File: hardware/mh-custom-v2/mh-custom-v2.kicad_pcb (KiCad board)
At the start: 2 copper layers, 95.7 x 99.3 mm, 113 parts, among them J1 Conn_01x03_Male, J10 Screw_Terminal_01x02, J11 Screw_Terminal_01x02, J12 Screw_Terminal_01x02, J3 Conn_02x19_Top_Bottom, J4 Conn_02x19_Top_Bottom, J5 Screw_Terminal_01x02, J6 Screw_Terminal_01x02, J7 Screw_Terminal_01x02, J8 Screw_Terminal_01x02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

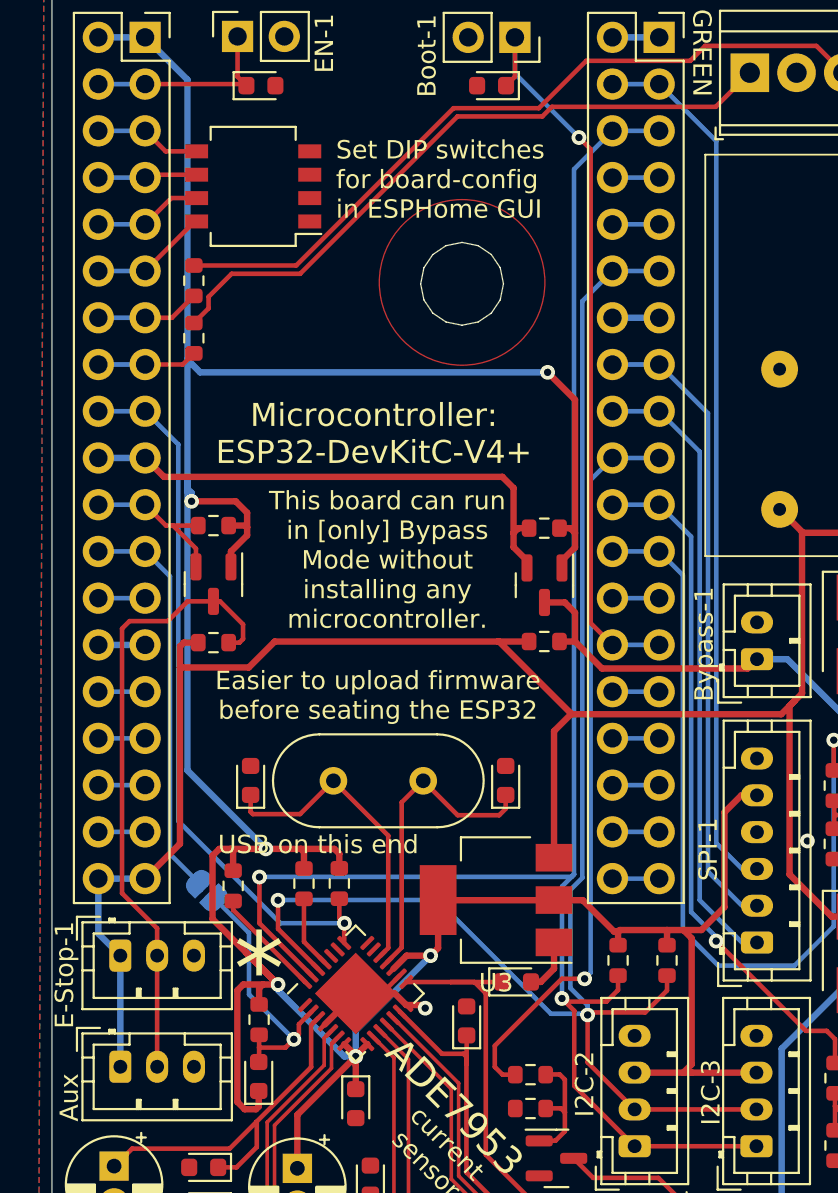
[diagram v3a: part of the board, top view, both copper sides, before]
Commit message: added jumpers that allow for two seperate E-Stop readings
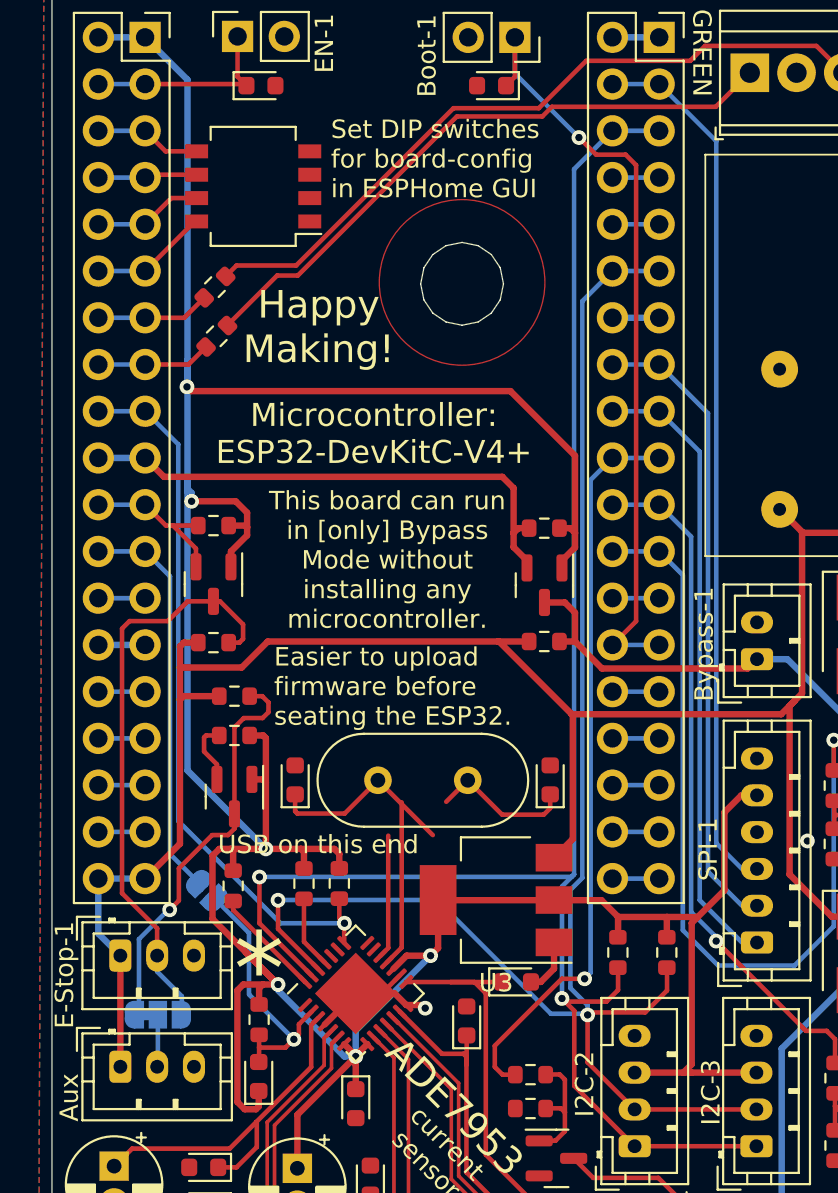
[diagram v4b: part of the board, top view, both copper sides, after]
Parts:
- added JP14: SolderJumper_3_Bridged12, Jumper:SolderJumper-3_P1.3mm_Bridged12_RoundedPad1.0x1.5mm, B.Cu at (38.7, 78.2)
- added R34: 10k, Resistor_SMD:R_0603_1608Metric, F.Cu at (42.9, 63.1)
- added R35: 10k, Resistor_SMD:R_0603_1608Metric, F.Cu at (42.9, 60.9)
- added T6: AO3400A, Package_TO_SOT_SMD:SOT-23, F.Cu at (42.9, 66.4)
- R7, R8: value 10kOhm -> 2.2k
- moved C20 2.42 mm to (46.2, 65.5)
- moved C21 2.42 mm to (60.0, 65.5)
- moved Y1 2.42 mm to (53.1, 65.5)
- moved R6 1.25 mm to (41.9, 41.4), turned to -135 degrees
- moved R5 1.20 mm to (41.8, 38.7), turned to 45 degrees
- moved R8 0.43 mm to (63.7, 74.9)
- moved R7 0.43 mm to (66.4, 74.9)
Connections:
- E-Stop-2 pad 2: Net-(E-Stop-1-Pad2) -> Net-(E-Stop-2-Pad2)
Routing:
- net Net-(JP14-Pad1): track 0.00 -> 22.3 mm, vias 0 -> 1
- net +3V3: track 194.4 -> 201.5 mm
- net read-aux-E-Stop: track 0.00 -> 3.44 mm
- net Net-(E-Stop-2-Pad2): track 0.00 -> 2.85 mm
- net +5V: track 162.2 -> 164.5 mm
- net Net-(E-Stop-1-Pad2): track 34.0 -> 31.7 mm
- net Net-(J1-Pad1): track 36.2 -> 34.1 mm
- net boot: track 40.6 -> 42.6 mm
- net Net-(J1-Pad3): track 40.9 -> 39.4 mm
- net led-grn: track 5.44 -> 6.58 mm
- net led-red: track 5.68 -> 6.20 mm
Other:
- board text added: "Easier to upload firmware before seating the ESP32."
- board text added: "Happy Making!"
- board text added: "also swap"
- board text removed: "Easier to upload firmware before seating the ESP32"

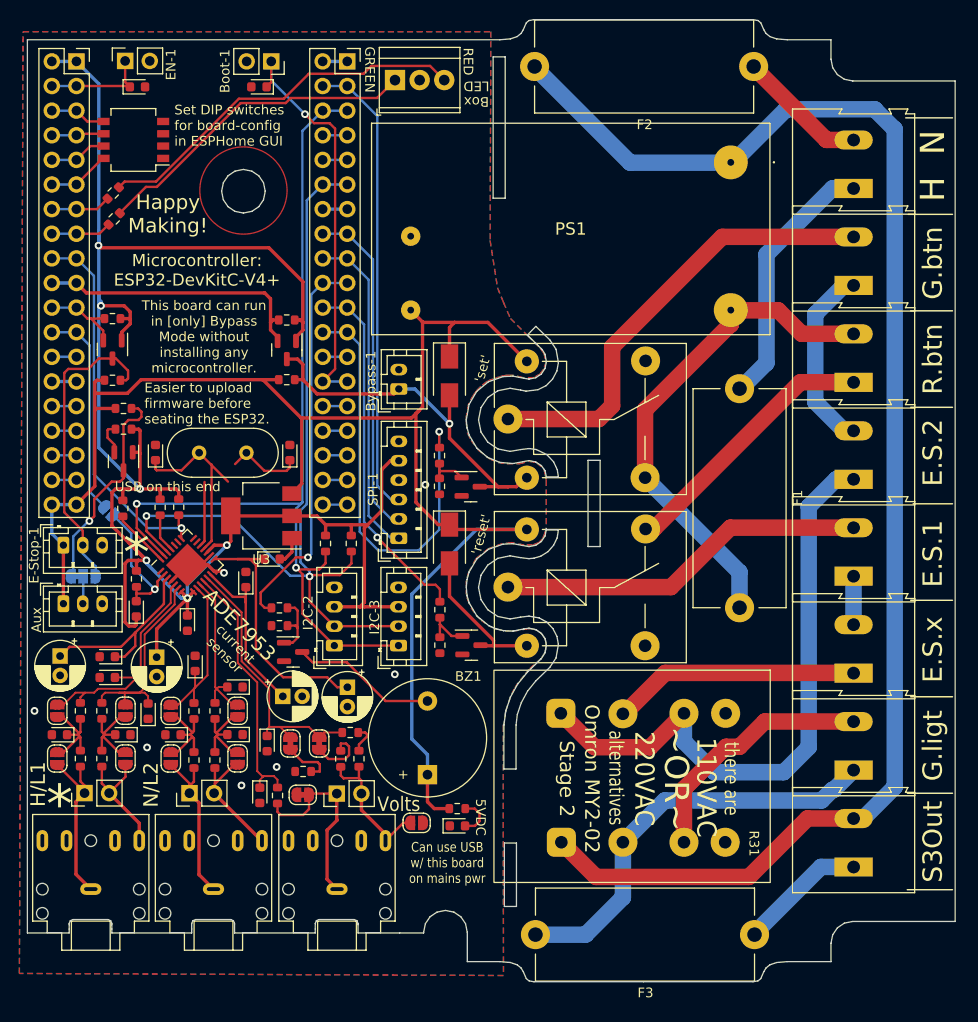
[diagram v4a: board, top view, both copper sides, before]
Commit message: b-silkscreen fixed
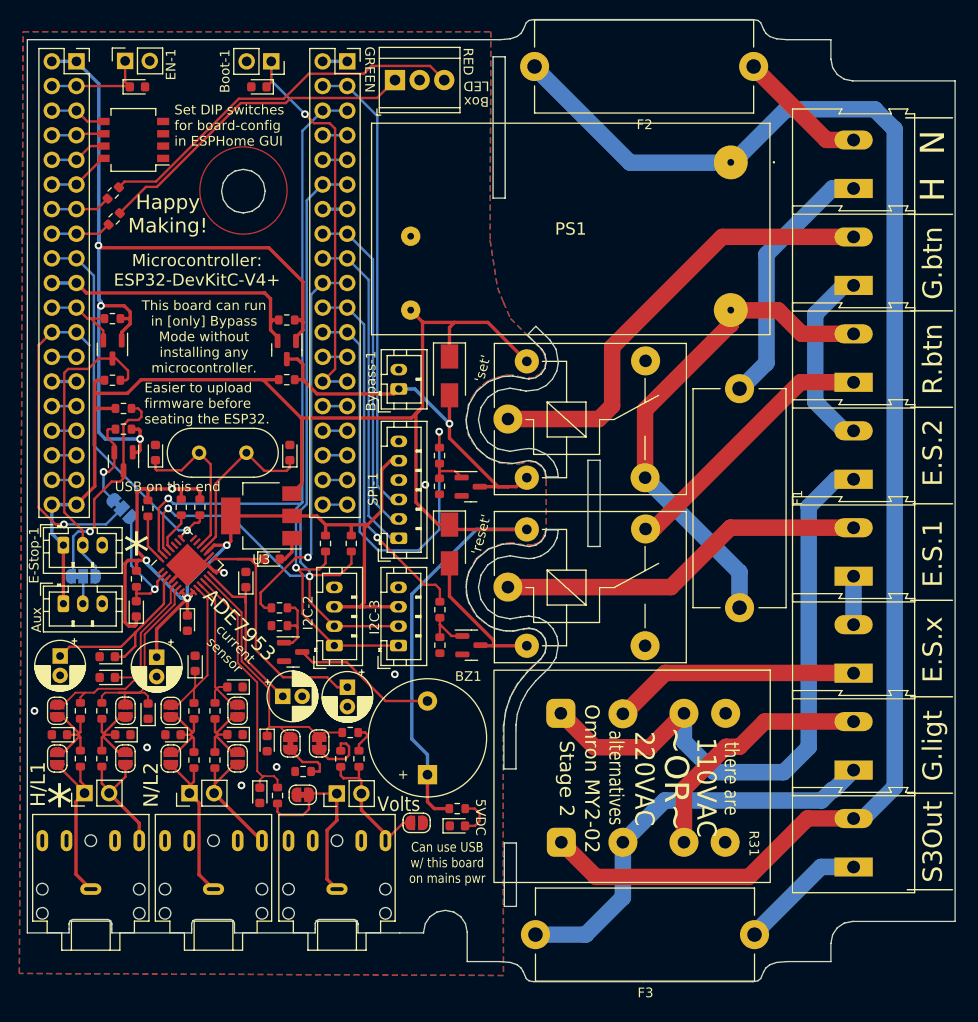
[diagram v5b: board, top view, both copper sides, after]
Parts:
- JP13: value software-reset -> SolderJumper_3_Bridged12; footprint Jumper:SolderJumper-2_P1.3mm_Open_RoundedPad1.0x1.5mm -> Jumper:SolderJumper-3_P1.3mm_Bridged12_RoundedPad1.0x1.5mm
- moved R24 2.59 mm to (45.4, 71.2)
- moved R23 2.18 mm to (50.7, 71.1)
- moved R25 2.18 mm to (48.8, 71.1)
- moved JP13 1.35 mm to (42.7, 71.2)
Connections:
- J3 pad 23: ade7953-reset -> two-options
- J3 pad 24: ade7953-reset -> two-options
- JP13 pad 1: ade7953-reset -> read-aux-E-Stop
- JP13 pad 2: Net-(C15-Pad2) -> two-options
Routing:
- net two-options: track 0.00 -> 33.1 mm, vias 0 -> 1
- net ade7953-reset: track 21.7 -> 0.00 mm
- net +3V3: track 201.5 -> 190.5 mm, vias 6 -> 7
- net read-aux-E-Stop: track 3.44 -> 9.50 mm, vias 0 -> 1
- net SCL: track 95.0 -> 92.0 mm
- net SDA: track 86.8 -> 85.2 mm
- net CS: track 6.02 -> 4.95 mm
- net Net-(C21-Pad1): track 16.8 -> 17.9 mm
- net Net-(C15-Pad2): track 14.8 -> 13.9 mm
- net Net-(JP14-Pad1): track 22.3 -> 23.0 mm
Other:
- board text added: "Read 2 EStops or ADE7953 reset"
- board text removed: "ADE7953 reset pin connect"

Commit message: applied workaround for 3.3v and 3v3 known bug: https://gitlab.com/kicad/libraries/kicad-symbols/-/issues/3153
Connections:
- C13 pad 1: +3V3 -> +3.3V
- C14 pad 1: +3V3 -> +3.3V
- C15 pad 1: +3V3 -> +3.3V
- I2C-2 pad 3: +3V3 -> +3.3V
- I2C-3 pad 3: +3V3 -> +3.3V
- J3 pad 1: +3V3 -> +3.3VA
- J3 pad 2: +3V3 -> +3.3VA
- R22 pad 2: +3V3 -> +3.3V
- R23 pad 2: +3V3 -> +3.3V
- R24 pad 2: +3V3 -> +3.3V
- R25 pad 2: +3V3 -> +3.3V
- R3 pad 2: +3V3 -> +3.3VA
- R32 pad 2: +3V3 -> +3.3VA
- R34 pad 2: +3V3 -> +3.3VA
- R7 pad 2: +3V3 -> +3.3V
- R8 pad 2: +3V3 -> +3.3V
- SPI-1 pad 5: +3V3 -> +3.3V
- T2 pad 1: +3V3 -> +3.3VA
- T5 pad 1: +3V3 -> +3.3VA
- T6 pad 1: +3V3 -> +3.3VA
- U2 pad 17: +3V3 -> +3.3V
- U2 pad 7: +3V3 -> +3.3V
- U2 pad 8: +3V3 -> +3.3V
- U3 pad 2: +3V3 -> +3.3V
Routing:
- net +3V3: track 190.5 -> 0.00 mm, vias 7 -> 0
- net +3.3V: track 0.00 -> 99.5 mm, vias 0 -> 3
- net +3.3VA: track 0.00 -> 90.2 mm, vias 0 -> 3
- net two-options: track 33.1 -> 31.2 mm
- net Net-(JP7-Pad1): track 6.87 -> 6.25 mm
- net GND: vias 7 -> 9
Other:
- board text added: "3 stages or relays WiFi microcontroller E-Stop integration Current Sensor"
- board text added: "Designed by: Corey Rice, Iris Artin,"
- board text added: "EStp1"
- board text added: "EStp2"
- board text added: "EStp3"
- board text added: "OUT"
- board text added: "Vincent, Lior, J.R., & Chris"
- board text removed: "Designed by: Corey Rice, Iris Artin, Vincent, Lior, J.R."
- board text removed: "E.S.1"
- board text removed: "E.S.2"
- board text removed: "E.S.x"
- board text removed: "S3Out"
